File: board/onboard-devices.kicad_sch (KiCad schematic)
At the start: 32 parts, among them Q1 DMG1012T, Q2 DMG1012T, Q3 DMG1012T, Q4 DMG1012T, SW1 SW_DIP_x08

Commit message: Change switches
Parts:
- removed SW1: SW_DIP_x08, Button_Switch_SMD:SW_DIP_SPSTx08_Slide_6.7x21.88mm_W6.73mm_P2.54mm_LowProfile_JPin, symbol Switch:SW_DIP_x08
- added SW1, SW2, SW3, SW4, SW5, SW6, SW7, SW8: MST22D18G2 125, HispalisFPGA:SW-SMD_MST22D18G2, symbol Switch:SW_Slide_DPDT
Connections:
- net +3V3: now also SW1.2 (B), SW2.2 (B), SW3.2 (B), SW4.2 (B), SW5.2 (B), SW6.2 (B), SW7.2 (B), SW8.2 (B)
- net SW1: now also SW1.1 (A)
- net SW2: now also SW2.1 (A)
- net SW3: now also SW3.1 (A)
- net SW4: now also SW4.1 (A)
- net SW5: now also SW5.1 (A)
- net SW6: now also SW6.1 (A)
- net SW7: now also SW7.1 (A)
- net SW8: now also SW8.1 (A)
- no-connect marks 0 -> 32
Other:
- moved on the sheet: BTN1, BTN2, BTN3, BTN4, BTN5, DISPLAY1, LD1, LD2, LD3, LD4, LD5, LD6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

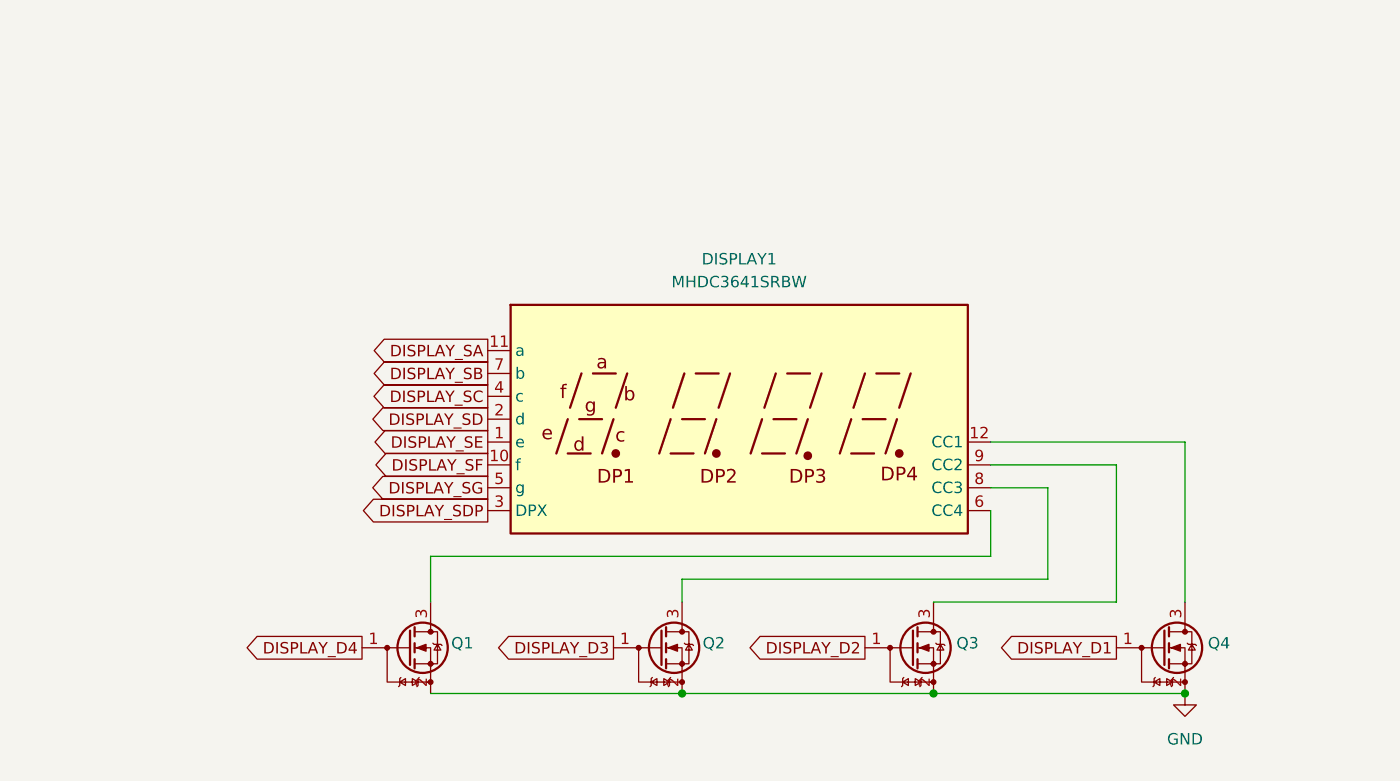
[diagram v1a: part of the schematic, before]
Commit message: Set display symbol and footprint from EasyEDA
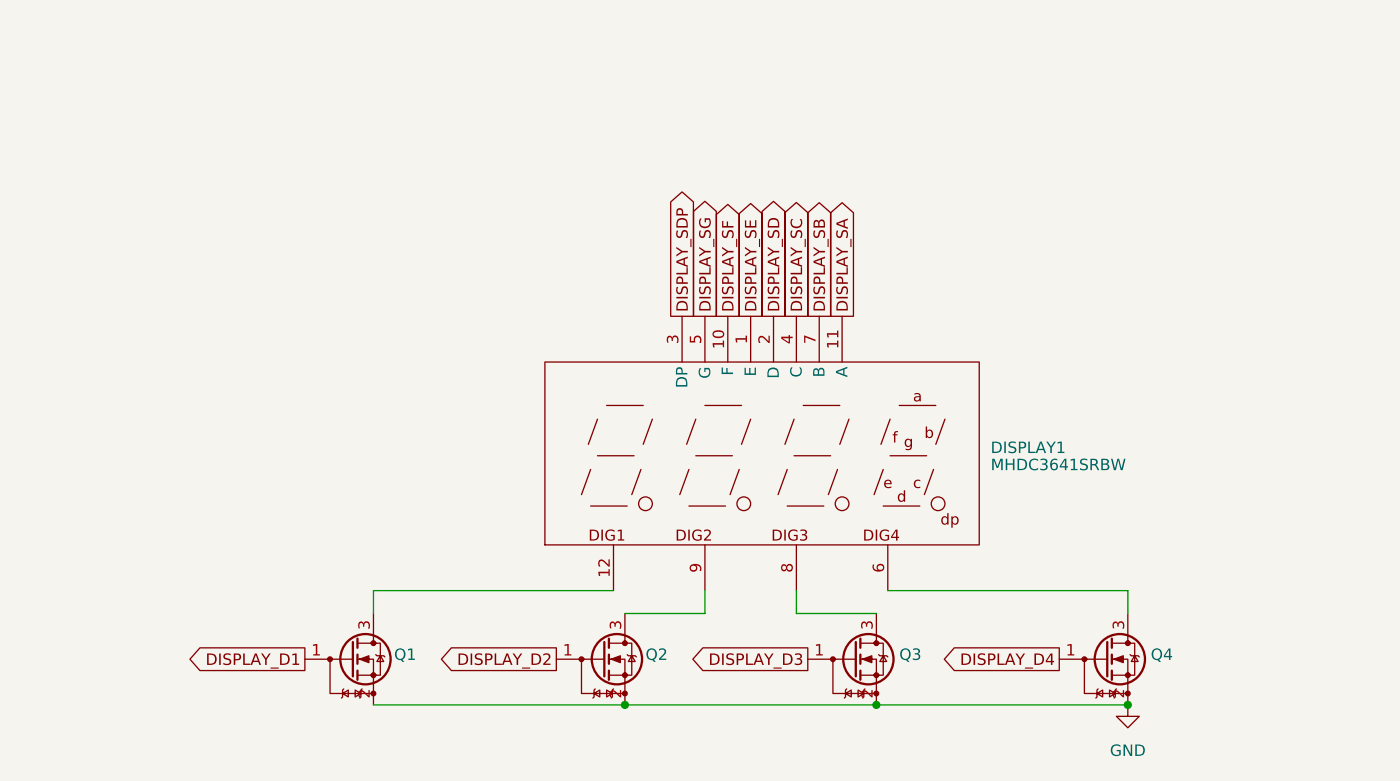
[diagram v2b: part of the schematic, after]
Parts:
- removed DISPLAY1: MHDC3641SRBW, HispalisFPGA:MHDC3641SRBW, symbol Display_Character:CC56-12SRWA
- added DISPLAY1: MHDC3641SRBW, HispalisFPGA:LED-SEG-TH_12P-L30.0-W14.0-P2.54-LS10.2, symbol MHDC3641SRBW:MHDC3641SRBW
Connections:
- net DISPLAY_D1: now also Q1.1 (G); no longer Q4.1 (G)
- net DISPLAY_D2: now also Q2.1 (G); no longer Q3.1 (G)
- net DISPLAY_D3: now also Q3.1 (G); no longer Q2.1 (G)
- net DISPLAY_D4: now also Q4.1 (G); no longer Q1.1 (G)
- net DISPLAY_SA: now also DISPLAY1.11 (A)
- net DISPLAY_SB: now also DISPLAY1.7 (B)
- net DISPLAY_SC: now also DISPLAY1.4 (C)
- net DISPLAY_SD: now also DISPLAY1.2 (D)
- net DISPLAY_SDP: now also DISPLAY1.3 (DP)
- net DISPLAY_SE: now also DISPLAY1.1 (E)
- net DISPLAY_SF: now also DISPLAY1.10 (F)
- net DISPLAY_SG: now also DISPLAY1.5 (G)
- net at Q1.3 (D): now also DISPLAY1.12 (DIG1)
- net at Q3.3 (D): now also DISPLAY1.8 (DIG3)
- net at Q2.3 (D): now also DISPLAY1.9 (DIG2)
- net at Q4.3 (D): now also DISPLAY1.6 (DIG4)
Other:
- moved on the sheet: Q1, Q2, Q3, Q4
